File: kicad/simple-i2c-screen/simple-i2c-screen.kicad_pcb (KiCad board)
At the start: 2 copper layers, 99.9 x 73.7 mm, 42 parts, among them J1 Barrel_Jack_MountingPin, J2 Conn_01x06, J3 Conn_01x01, J4 RJ12, J5 Conn_01x01, J6 Conn_01x01, J7 Conn_01x01, J8 Conn_02x03_Odd_Even, SW2 Rotary_Encoder_Switch, U1 LM78M05_TO252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

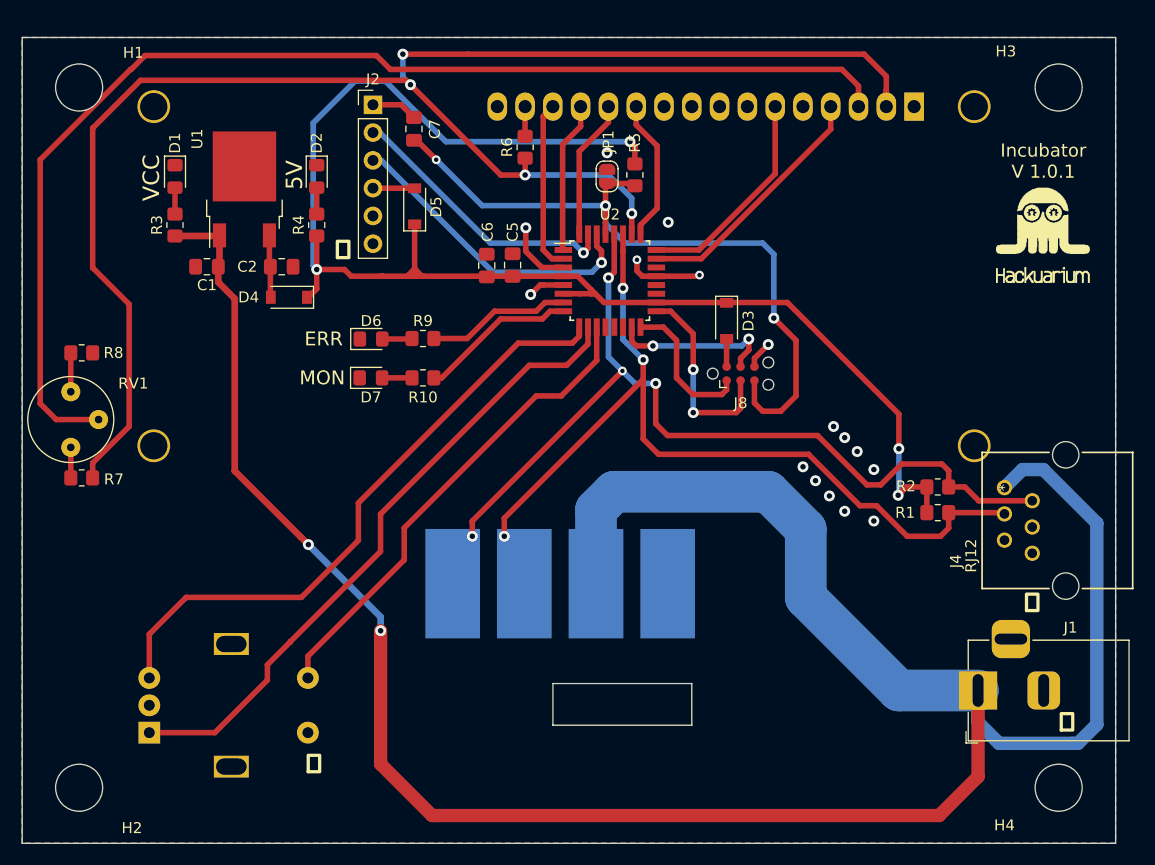
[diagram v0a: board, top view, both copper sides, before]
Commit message: fix: version 1.0.2 of the PCB change size holes M4 -> M3 and changes their position
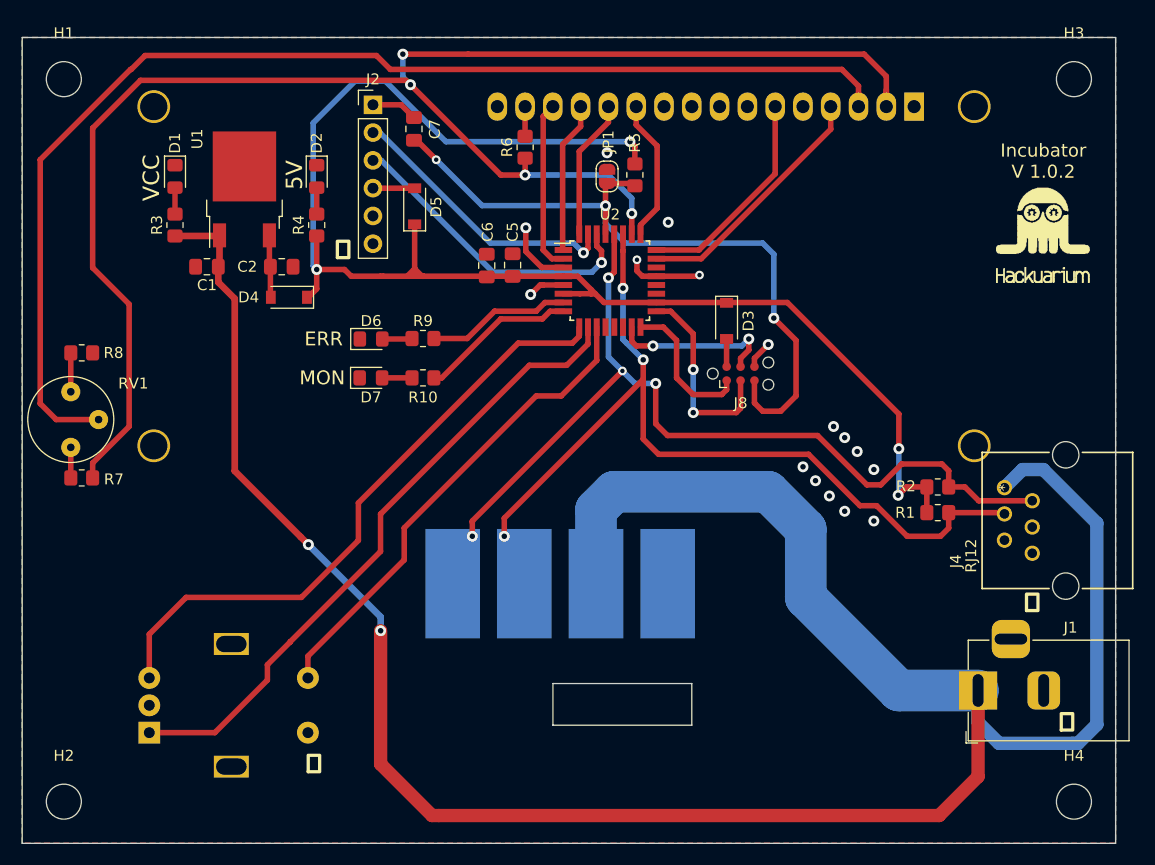
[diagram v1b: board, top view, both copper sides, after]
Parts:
- H1, H2, H3, H4: footprint MountingHole:MountingHole_4.3mm_M4 -> MountingHole:MountingHole_3.2mm_M3
- moved H2 1.89 mm to (3.81, -3.81)
- moved H4 1.89 mm to (96.1, -3.81)
- moved H1 1.59 mm to (3.81, -69.8)
- moved H3 1.59 mm to (96.1, -69.8)
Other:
- board text added: "Incubator V 1.0.2"
- board text removed: "Incubator V 1.0.1"

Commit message: refactor: version 1.0.3 for PCB change MOITORING_LED to pin 13 like Arduino
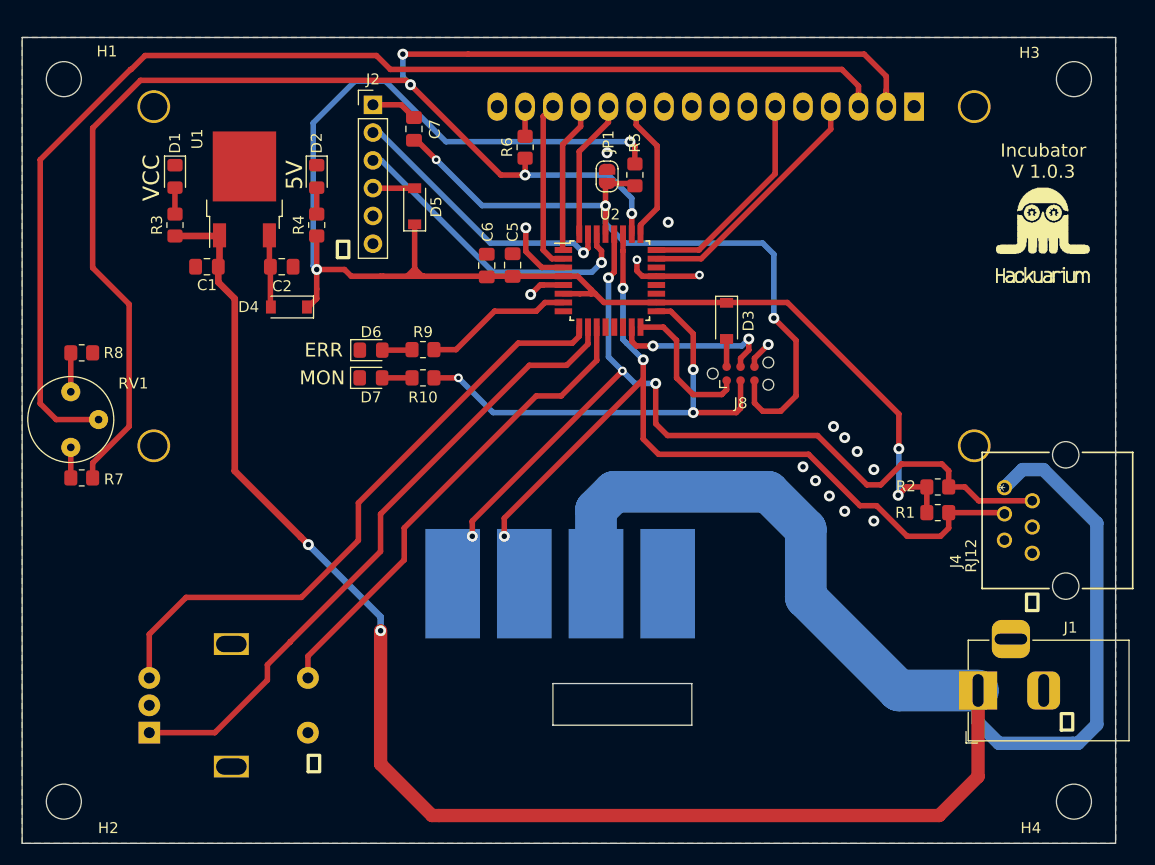
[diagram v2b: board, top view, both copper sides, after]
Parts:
- moved D6 1.02 mm to (31.9, -45.1)
- moved R9 1.02 mm to (36.6, -45.1)
- moved D4 0.89 mm to (24.4, -49.0)
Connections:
- J8 pad 3: SCK -> SCK|MONITORING
- R10 pad 1: MONITORING -> SCK|MONITORING
- U2 pad 17: SCK -> SCK|MONITORING
- U2 pad 8: MONITORING -> Net-(U2-Pad8)
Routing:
- net SCK|MONITORING: track 0.00 -> 43.5 mm, vias 0 -> 3
- net SCK: track 18.5 -> 0.00 mm, vias 2 -> 0
- net MONITORING: track 14.4 -> 0.00 mm
- net VIN: track 136.8 -> 137.6 mm
- net Net-(C2-Pad1): track 5.72 -> 6.61 mm
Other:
- board text added: "Incubator V 1.0.3"
- board text removed: "Incubator V 1.0.2"
